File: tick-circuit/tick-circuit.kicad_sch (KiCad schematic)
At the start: 10 parts, among them J1 Power, J2 50/60 Hz Output, U2 74HCT73, U4 74HCT4060, X1 3.93216 MHz

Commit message: First round of PCB, but no idea what I am doing
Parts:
- C1, C2, C3: footprint Capacitor_THT:C_Disc_D7.0mm_W2.5mm_P5.00mm -> Capacitor_THT:C_Disc_D4.7mm_W2.5mm_P5.00mm
- J2: value 50/60 Hz Output -> 50/60Hz
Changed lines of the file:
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@@
       (effects (font (size 1.27 1.27)) (justify left))
     )
-    (property "Value" "50/60 Hz Output" (at 160.02 49.53 0)
+    (property "Value" "50/60Hz " (at 160.02 49.53 0)
       (effects (font (size 1.27 1.27)) (justify left))
     )
@@
       (effects (font (size 1.27 1.27)) (justify left))
     )
-    (property "Footprint" "Capacitor_THT:C_Disc_D7.0mm_W2.5mm_P5.00mm" (at 44.1452 71.12 0)
+    (property "Footprint" "Capacitor_THT:C_Disc_D4.7mm_W2.5mm_P5.00mm" (at 44.1452 71.12 0)
       (effects (font (size 1.27 1.27)) hide)
     )
@@
       (effects (font (size 1.27 1.27)) (justify left))
     )
-    (property "Footprint" "Capacitor_THT:C_Disc_D7.0mm_W2.5mm_P5.00mm" (at 61.9252 71.12 0)
+    (property "Footprint" "Capacitor_THT:C_Disc_D4.7mm_W2.5mm_P5.00mm" (at 61.9252 71.12 0)
       (effects (font (size 1.27 1.27)) hide)
     )
@@
       (effects (font (size 1.27 1.27)) (justify left))
     )
-    (property "Footprint" "Capacitor_THT:C_Disc_D7.0mm_W2.5mm_P5.00mm" (at 100.0252 26.67 0)
-      (effects (font (size 1.27 1.27)) hide)
-    )
+    (property "Footprint" "Capacitor_THT:C_Disc_D4.7mm_W2.5mm_P5.00mm" (at 100.0252 26.67 0)
+      (effects (font (size 1.27 1.27)) hide)
+    )

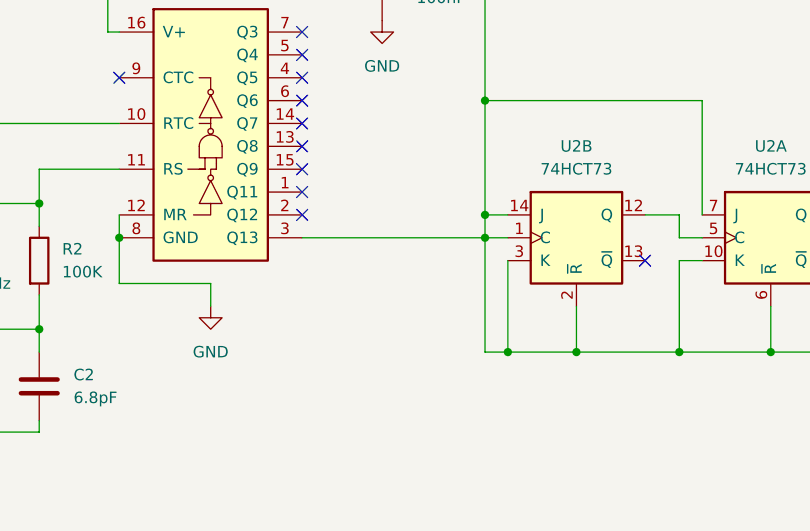
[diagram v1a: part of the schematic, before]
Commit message: Misconnected +5v to the connection from U1 to U2, which would have sucked
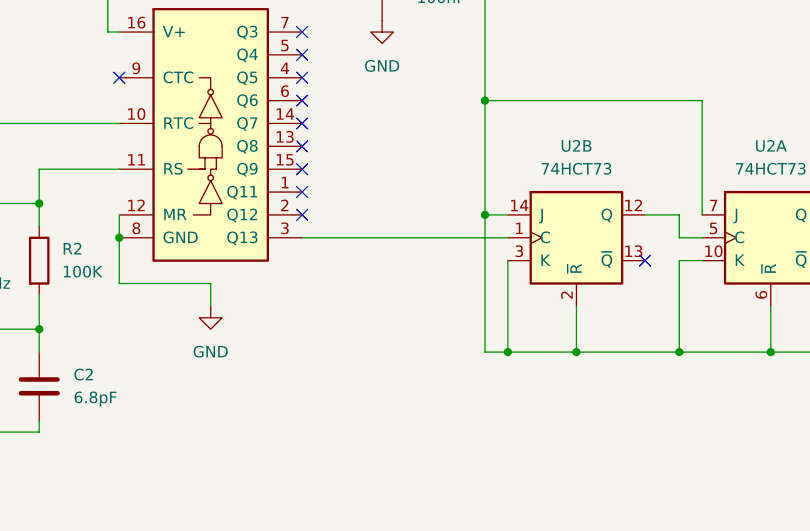
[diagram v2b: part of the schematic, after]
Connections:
- net +5V: no longer U2.1 (C), U4.3 (Q13)
- new net: U2.1 (C), U4.3 (Q13)
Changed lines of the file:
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@@
     (comment 2 "For 50Hz, replace X1 with 3.2768 MHz")
-  )
-  (junction (at 110.49 50.8) (diameter 0) (color 0 0 0 0)
   )
   (junction (at 113.03 63.5) (diameter 0) (color 0 0 0 0)
@@
   )
   (wire (pts (xy 142.24 63.5) (xy 153.67 63.5))
-    (stroke (width 0) (type default))
-  )
-  (wire (pts (xy 110.49 50.8) (xy 113.03 50.8))
     (stroke (width 0) (type default))
   )
@@
     (stroke (width 0) (type default))
   )
-  (wire (pts (xy 90.17 50.8) (xy 110.49 50.8))
+  (wire (pts (xy 90.17 50.8) (xy 113.03 50.8))
     (stroke (width 0) (type default))
   )
@@
     (stroke (width 0) (type default))
   )
-  (wire (pts (xy 110.49 50.8) (xy 110.49 48.26))
-    (stroke (width 0) (type default))
-  )
   (wire (pts (xy 68.58 27.94) (xy 69.85 27.94))
     (stroke (width 0) (type default))
@@
     (stroke (width 0) (type default))
   )
-  (wire (pts (xy 110.49 63.5) (xy 110.49 50.8))
+  (wire (pts (xy 110.49 48.26) (xy 110.49 63.5))
     (stroke (width 0) (type default))
   )

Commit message: Change resistor footprints, change J2 footprint, alter routing to match, move 5v away from gnd, add URL to pcb
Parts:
- J2: footprint Connector_PinHeader_1.00mm:PinHeader_1x01_P1.00mm_Horizontal -> Connector_PinHeader_2.00mm:PinHeader_1x01_P2.00mm_Horizontal
- R1, R2: footprint Resistor_THT:R_Axial_DIN0204_L3.6mm_D1.6mm_P5.08mm_Horizontal -> Resistor_THT:R_Axial_DIN0207_L6.3mm_D2.5mm_P7.62mm_Horizontal
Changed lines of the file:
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@@
       (effects (font (size 1.27 1.27)) (justify left))
     )
-    (property "Footprint" "Connector_PinHeader_1.00mm:PinHeader_1x01_P1.00mm_Horizontal" (at 158.75 48.26 0)
+    (property "Footprint" "Connector_PinHeader_2.00mm:PinHeader_1x01_P2.00mm_Horizontal" (at 158.75 48.26 0)
       (effects (font (size 1.27 1.27)) hide)
     )
@@
       (effects (font (size 1.27 1.27)))
     )
-    (property "Footprint" "Resistor_THT:R_Axial_DIN0204_L3.6mm_D1.6mm_P5.08mm_Horizontal" (at 52.07 48.768 90)
+    (property "Footprint" "Resistor_THT:R_Axial_DIN0207_L6.3mm_D2.5mm_P7.62mm_Horizontal" (at 52.07 48.768 90)
       (effects (font (size 1.27 1.27)) hide)
     )
@@
       (effects (font (size 1.27 1.27)) (justify left))
     )
-    (property "Footprint" "Resistor_THT:R_Axial_DIN0204_L3.6mm_D1.6mm_P5.08mm_Horizontal" (at 59.182 53.34 90)
-      (effects (font (size 1.27 1.27)) hide)
-    )
+    (property "Footprint" "Resistor_THT:R_Axial_DIN0207_L6.3mm_D2.5mm_P7.62mm_Horizontal" (at 59.182 53.34 90)
+      (effects (font (size 1.27 1.27)) hide)
+    )

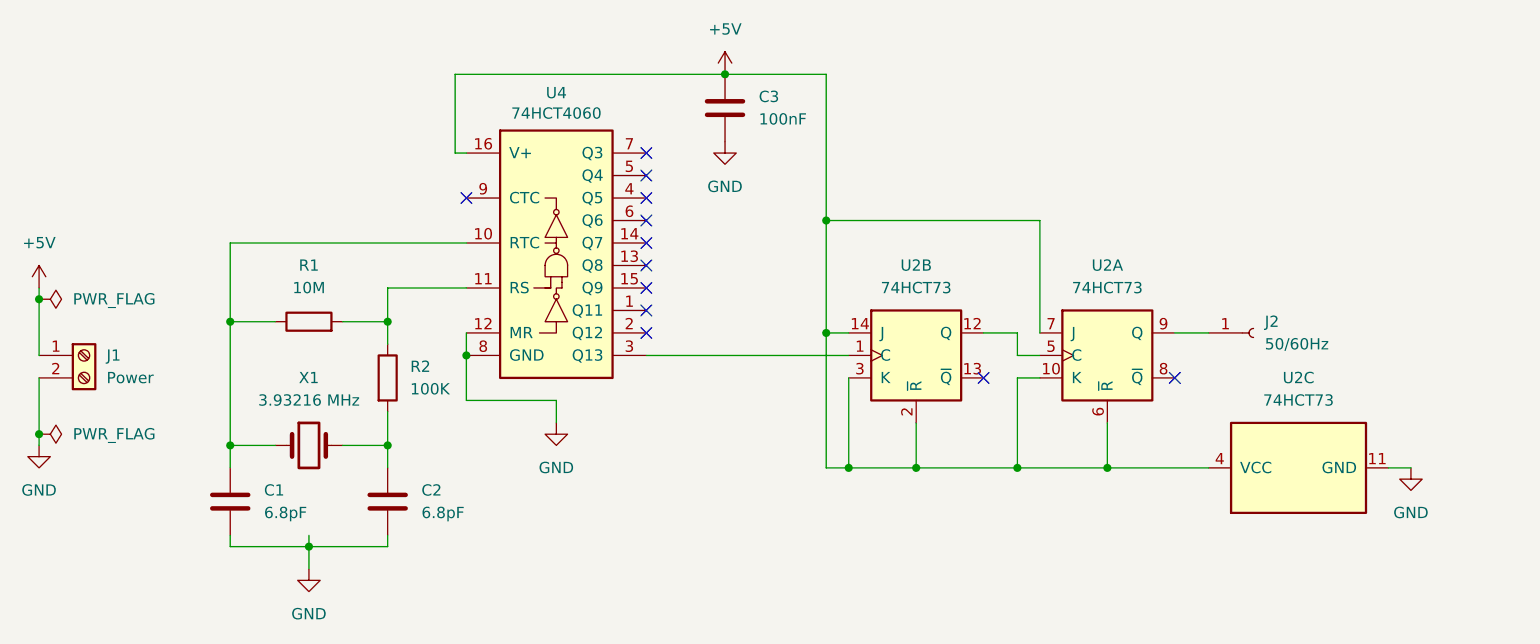
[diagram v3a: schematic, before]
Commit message: Tick Circuit v2, an altered layout of the board to fit the electrical paths better
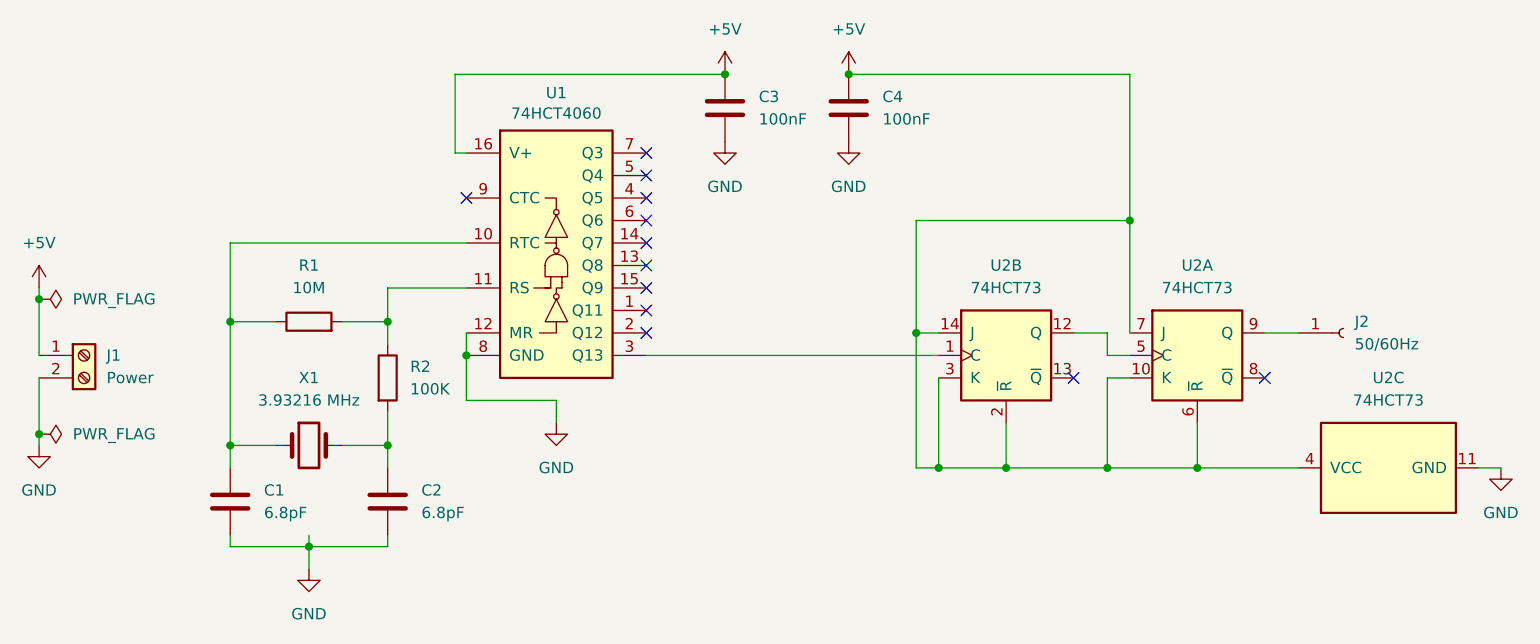
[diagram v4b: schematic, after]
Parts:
- added C4: 100nF, Capacitor_THT:C_Disc_D4.7mm_W2.5mm_P5.00mm, symbol Device:C
- J2: value 50/60Hz -> 50/60Hz; footprint Connector_PinHeader_2.00mm:PinHeader_1x01_P2.00mm_Horizontal -> TerminalBlock_MetzConnect:TerminalBlock_MetzConnect_360272_1x01_Horizontal_ScrewM2.6
- renumbered U4 to U1
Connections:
- net +5V: now also C4.1
- net GND: now also C4.2
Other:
- moved on the sheet: J2, U2A, U2B, U2C

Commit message: Update resistor footprint to hold a larger one, update README to show test success
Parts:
- R1, R2: footprint Resistor_THT:R_Axial_DIN0207_L6.3mm_D2.5mm_P7.62mm_Horizontal -> Resistor_THT:R_Axial_DIN0207_L6.3mm_D2.5mm_P10.16mm_Horizontal
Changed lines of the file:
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@@
 			)
 		)
-		(property "Footprint" "Resistor_THT:R_Axial_DIN0207_L6.3mm_D2.5mm_P7.62mm_Horizontal"
+		(property "Footprint" "Resistor_THT:R_Axial_DIN0207_L6.3mm_D2.5mm_P10.16mm_Horizontal"
 			(at 52.07 48.768 90)
 			(effects
@@
 			)
 		)
-		(property "Footprint" "Resistor_THT:R_Axial_DIN0207_L6.3mm_D2.5mm_P7.62mm_Horizontal"
+		(property "Footprint" "Resistor_THT:R_Axial_DIN0207_L6.3mm_D2.5mm_P10.16mm_Horizontal"
 			(at 59.182 53.34 90)
 			(effects
